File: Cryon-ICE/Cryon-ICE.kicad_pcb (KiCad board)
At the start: 4 copper layers, 34.3 x 63 mm, 207 parts, among them J101 Conn_02x32_Row_Letter_First, J302 10155435-00011LF, J501 TC2050, Q301 DMG1012T, U101 MPFS025T-FCVG484I, U301 PTN5150AHXMP, U302 USB3340-EZK-TR, U303 TPS2051BDR, U401 74LVC1G125, U402 74LVC1G125, U403 74LVC1G125, U404 74LVC1G125, U405 74LVC1G125, U406 74LVC1G125, U407 74LVC1G125, U408 74LVC1G125, U409 74LVC1G125, U410 74LVC1G125, U411 74LVC1G125, U412 74LVC1G125, U413 74LVC1G125, U414 74LVC1G125, U415 74LVC1G125, U416 74LVC1G125, U417 74LVC1G125, U418 74LVC1G125, U419 74LVC1G125, U420 74LVC1G125, U421 74LVC1G125, U422 74LVC1G125, U423 74LVC1G125, U424 74LVC1G125, U425 74LVC1G125, U426 74LVC1G125, U427 74LVC1G125, U428 74LVC1G125, U429 74LVC1G125, U430 74LVC1G125, U431 74LVC1G125, U432 74LVC1G125, U433 74LVC1G125, U434 74LVC1G125, U435 74LVC1G125, U436 74LVC1G125, U437 74LVC1G125, U438 74LVC1G125, U439 74LVC1G125, U440 74LVC1G125, U441 74LVC1G125, U442 74LVC1G125, U443 74LVC1G125, U444 74LVC1G125, U445 74LVC1G125, U446 74LVC1G125, U447 74LVC1G125, U448 74LVC1G125, U449 74LVC1G125, U450 74LVC1G125, U451 74LVC1G125, U452 74LVC1G125, U453 74LVC1G125, U454 74LVC1G125, U455 74LVC1G125, U456 74LVC1G125, U457 74LVC1G125, U458 74LVC1G125, U459 74LVC1G125, U460 74LVC1G125, U461 74LVC1G125, U462 74LVC1G125, U463 74LVC1G125, U464 74LVC1G125, U501 W25Q128JVS, U601 D1621XM4CDGVI-U, Y301 12.88481

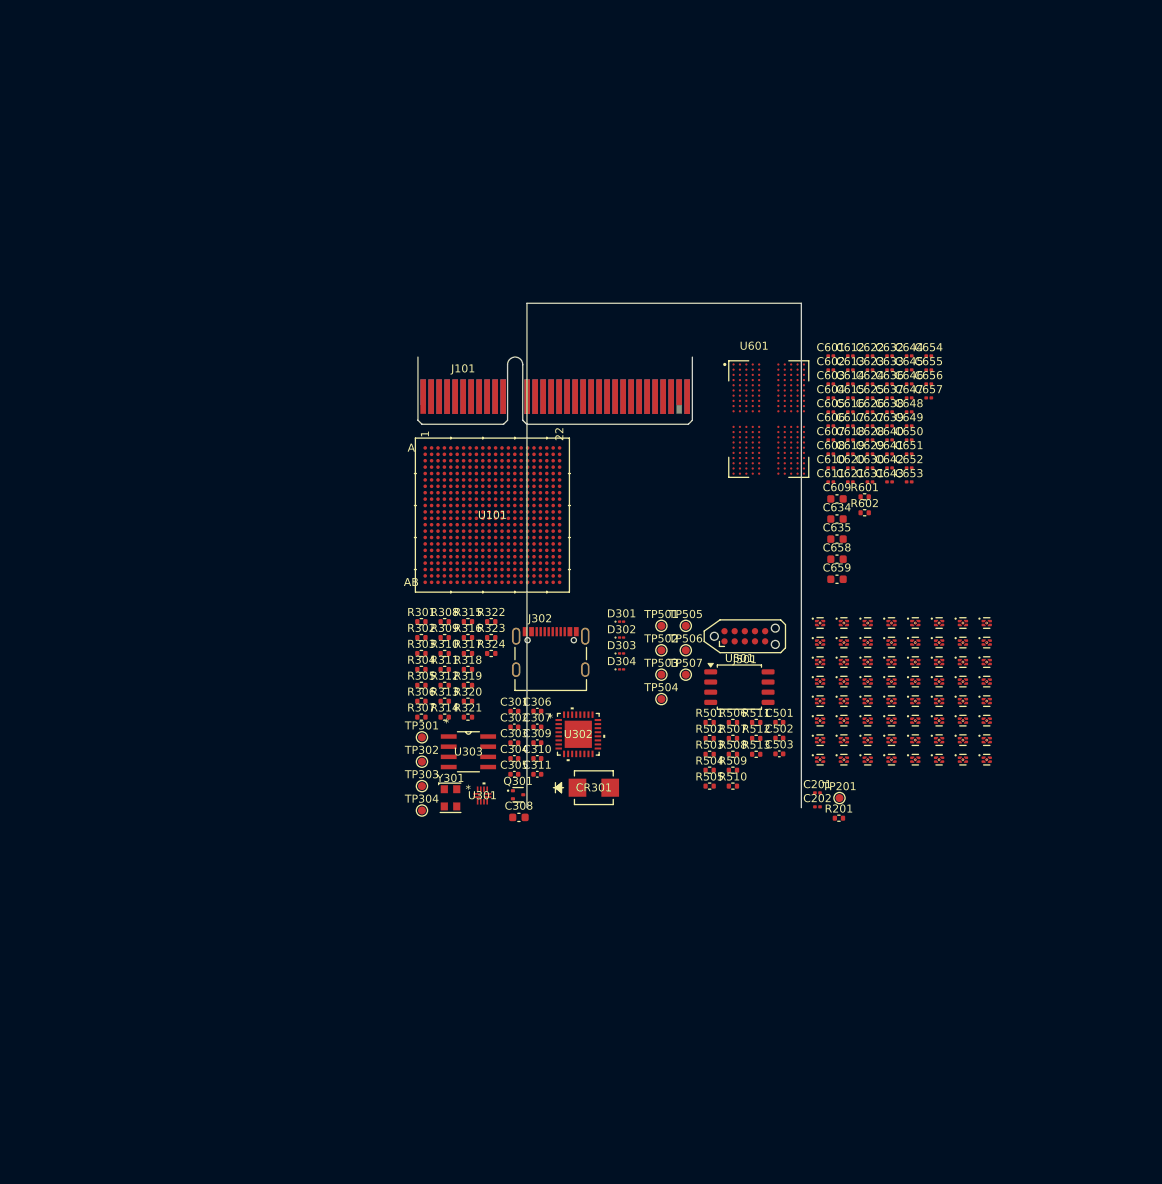
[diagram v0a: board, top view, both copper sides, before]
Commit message: Added micro-sd to schematic
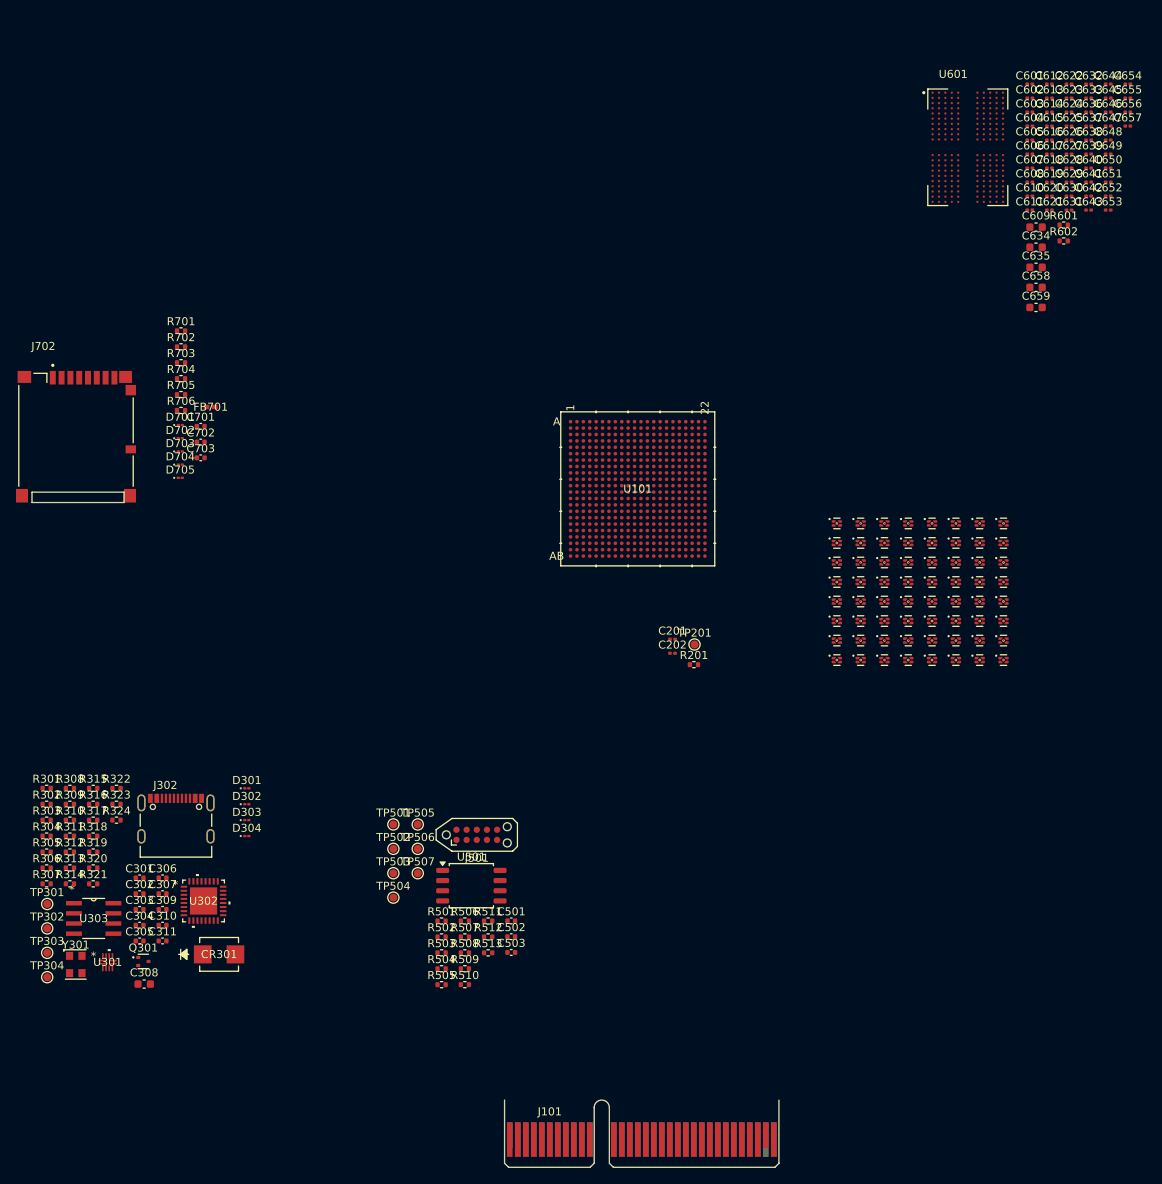
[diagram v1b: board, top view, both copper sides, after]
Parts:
- added C701: 1uF, Capacitor_SMD:C_0402_1005Metric, F.Cu at (89.8, 92.6)
- added C702: 100nF, Capacitor_SMD:C_0402_1005Metric, F.Cu at (89.8, 94.5)
- added C703: 100nF, Capacitor_SMD:C_0402_1005Metric, F.Cu at (89.8, 96.5)
- added D701: GSEPD15B0005, Cryon_Library:D_GSEPD15B0005_01005_0402Metric, F.Cu at (87.2, 92.4)
- added D702: GSEPD15B0005, Cryon_Library:D_GSEPD15B0005_01005_0402Metric, F.Cu at (87.2, 94.1)
- added D703: GSEPD15B0005, Cryon_Library:D_GSEPD15B0005_01005_0402Metric, F.Cu at (87.2, 95.7)
- added D704: GSEPD15B0005, Cryon_Library:D_GSEPD15B0005_01005_0402Metric, F.Cu at (87.2, 97.4)
- added D705: GSEPD15B0005, Cryon_Library:D_GSEPD15B0005_01005_0402Metric, F.Cu at (87.2, 99.0)
- added FB701: 120R-1.3A;0402, Cryon_Library:BLM15P_FBD, F.Cu at (91.0, 90.2)
- added J702: MSD-7-A, Cryon_Library:CUI_MSD-7-A, F.Cu at (74.2, 94.0)
- added R701: 10k, Resistor_SMD:R_0402_1005Metric, F.Cu at (87.3, 80.7)
- added R702: 10k, Resistor_SMD:R_0402_1005Metric, F.Cu at (87.3, 82.6)
- added R703: 10k, Resistor_SMD:R_0402_1005Metric, F.Cu at (87.3, 84.6)
- added R704: 10k, Resistor_SMD:R_0402_1005Metric, F.Cu at (87.3, 86.6)
- added R705: 10k, Resistor_SMD:R_0402_1005Metric, F.Cu at (87.3, 88.6)
- added R706: 33R, Resistor_SMD:R_0402_1005Metric, F.Cu at (87.3, 90.6)
- moved J101 93.5 mm to (128.4, 181.8)
- moved J302 51.3 mm to (86.7, 143.8)
- moved U301 51.3 mm to (78.1, 159.6)
- moved U302 51.3 mm to (90.1, 151.9)
- moved C301 51.3 mm to (82.1, 149.0)
- moved C302 51.3 mm to (82.1, 151.0)
- moved C303 51.3 mm to (82.1, 153.0)
- moved C304 51.3 mm to (82.1, 154.9)
- moved C305 51.3 mm to (82.1, 156.9)
- moved C306 51.3 mm to (85.0, 149.0)
- moved C307 51.3 mm to (85.0, 151.0)
- moved C309 51.3 mm to (85.0, 153.0)
- moved C310 51.3 mm to (85.0, 154.9)
- moved C311 51.3 mm to (85.0, 156.9)
- moved CR301 51.3 mm to (92.1, 158.6)
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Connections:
- U101 pad A2: unconnected-(U101E-MSSIO33B2-PadA2) -> /eMMC_SD/ADC_MISO
- U101 pad B2: unconnected-(U101E-MSSIO32B2-PadB2) -> /eMMC_SD/ADC_MOSI
- U101 pad C7: unconnected-(U101B-GPIO39NB1-PadC7) -> /SD_DET
- U101 pad E5: unconnected-(U101E-MSSIO30B2-PadE5) -> /eMMC_SD/ADC_SCK
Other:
- board size 34.3 x 63 mm -> 34.3 x 8.4 mm

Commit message: Added eMMC
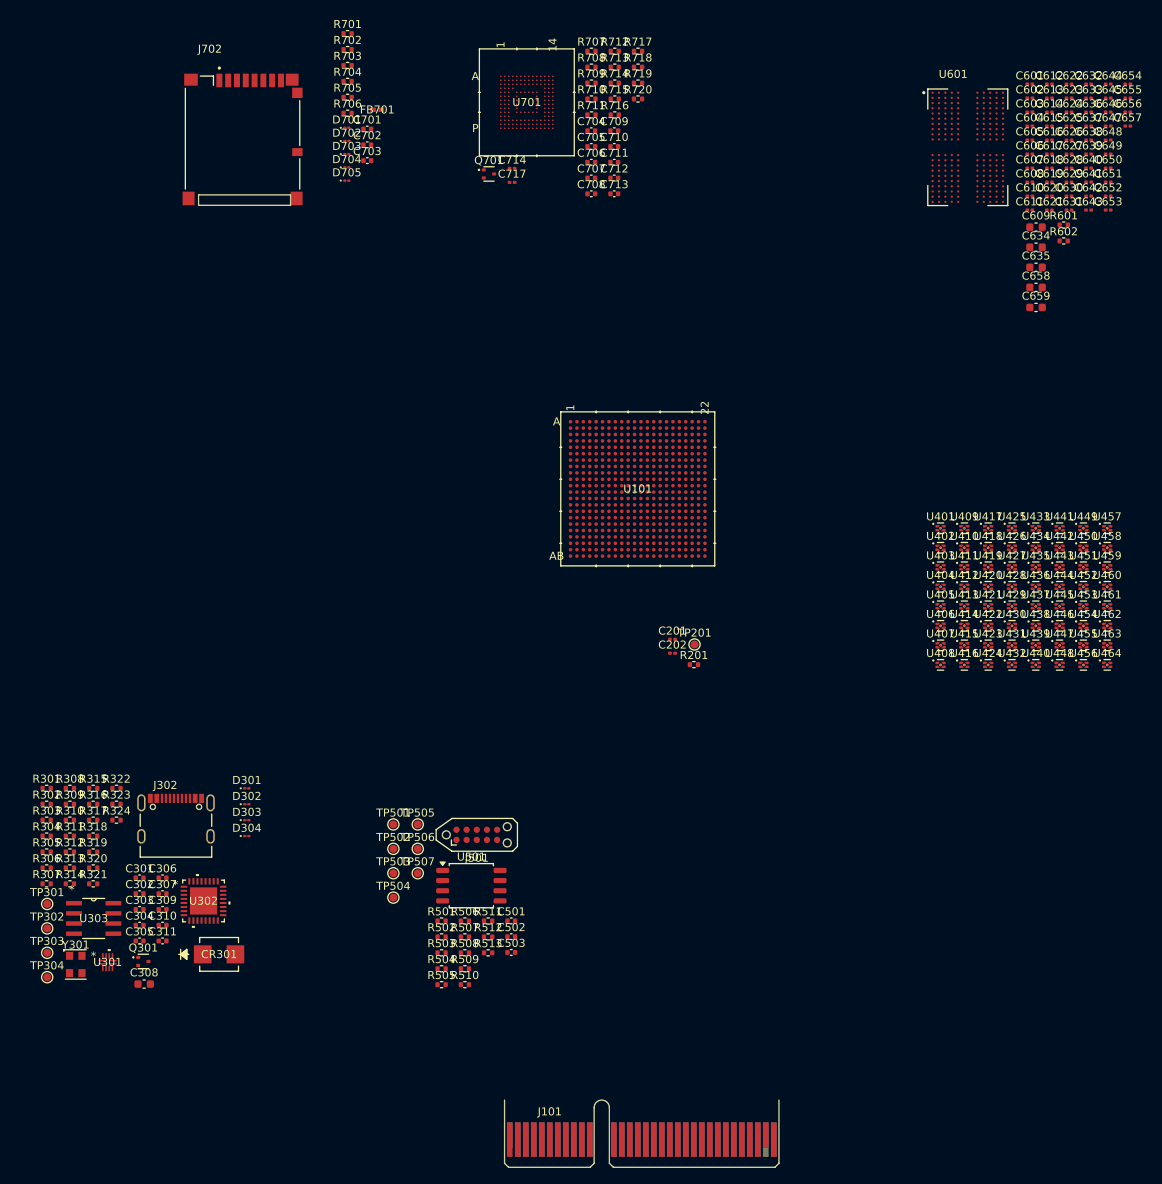
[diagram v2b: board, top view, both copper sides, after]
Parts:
- added C704: 100nF, Capacitor_SMD:C_0402_1005Metric, F.Cu at (138.6, 55.6)
- added C705: 100nF, Capacitor_SMD:C_0402_1005Metric, F.Cu at (138.6, 57.6)
- added C706: 100nF, Capacitor_SMD:C_0402_1005Metric, F.Cu at (138.6, 59.6)
- added C707: 100nF, Capacitor_SMD:C_0402_1005Metric, F.Cu at (138.6, 61.5)
- added C708: 100nF, Capacitor_SMD:C_0402_1005Metric, F.Cu at (138.6, 63.5)
- added C709: 100nF, Capacitor_SMD:C_0402_1005Metric, F.Cu at (141.5, 55.6)
- added C710: 100nF, Capacitor_SMD:C_0402_1005Metric, F.Cu at (141.5, 57.6)
- added C711: 100nF, Capacitor_SMD:C_0402_1005Metric, F.Cu at (141.5, 59.6)
- added C712: 100nF, Capacitor_SMD:C_0402_1005Metric, F.Cu at (141.5, 61.5)
- added C713: 100nF, Capacitor_SMD:C_0402_1005Metric, F.Cu at (141.5, 63.5)
- added C714: 4.7uF, Capacitor_SMD:C_0201_0603Metric, F.Cu at (128.7, 60.3)
- added C717: 4.7uF, Capacitor_SMD:C_0201_0603Metric, F.Cu at (128.7, 62.1)
- added Q701: DMG1012T, Cryon_Library:DMG1012-SOT-523, F.Cu at (125.8, 61.0)
- added R707: 10k, Resistor_SMD:R_0402_1005Metric, F.Cu at (138.6, 45.7)
- added R708: 10k, Resistor_SMD:R_0402_1005Metric, F.Cu at (138.6, 47.7)
- added R709: 49.9k, Resistor_SMD:R_0402_1005Metric, F.Cu at (138.6, 49.7)
- added R710: 49.9k, Resistor_SMD:R_0402_1005Metric, F.Cu at (138.6, 51.7)
- added R711: 49.9k, Resistor_SMD:R_0402_1005Metric, F.Cu at (138.6, 53.7)
- added R712: 49.9k, Resistor_SMD:R_0402_1005Metric, F.Cu at (141.5, 45.7)
- added R713: 49.9k, Resistor_SMD:R_0402_1005Metric, F.Cu at (141.5, 47.7)
- added R714: 49.9k, Resistor_SMD:R_0402_1005Metric, F.Cu at (141.5, 49.7)
- added R715: 49.9k, Resistor_SMD:R_0402_1005Metric, F.Cu at (141.5, 51.7)
- added R716: 49.9k, Resistor_SMD:R_0402_1005Metric, F.Cu at (141.5, 53.7)
- added R717: 49.9k, Resistor_SMD:R_0402_1005Metric, F.Cu at (144.4, 45.7)
- added R718: 49.9k, Resistor_SMD:R_0402_1005Metric, F.Cu at (144.4, 47.7)
- added R719: 0R, Resistor_SMD:R_0402_1005Metric, F.Cu at (144.4, 49.7)
- added R720: 10K, Resistor_SMD:R_0402_1005Metric, F.Cu at (144.4, 51.7)
- added U701: MX52LM08A11XVI, Cryon_Library:153BGA_11p5x13x1_MAC, F.Cu at (130.5, 52.1)
- moved C701 42.6 mm to (110.6, 55.4)
- moved R701 42.6 mm to (108.1, 43.5)
- moved C702 42.6 mm to (110.6, 57.4)
- moved C703 42.6 mm to (110.6, 59.4)
- moved D701 42.6 mm to (108.0, 55.3)
- moved D703 42.6 mm to (108.0, 58.6)
- moved D704 42.6 mm to (108.0, 60.2)
- moved FB701 42.6 mm to (111.8, 53.0)
- moved J702 42.6 mm to (95.0, 56.8)
- moved R702 42.6 mm to (108.1, 45.5)
- moved R704 42.6 mm to (108.1, 49.5)
- moved R705 42.6 mm to (108.1, 51.5)
- moved D702 42.6 mm to (108.0, 56.9)
- moved D705 42.6 mm to (108.0, 61.9)
- moved R703 42.6 mm to (108.1, 47.5)
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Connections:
- J702 pad SW_A2: /SD_DET -> GND
- U101 pad H1: unconnected-(U101E-MSSIO2B4-PadH1) -> /eMMC_SD/EMMC_DATA0
- U101 pad H2: unconnected-(U101E-MSSIO11B4-PadH2) -> /eMMC_SD/EMMC_DATA7
- U101 pad H4: unconnected-(U101E-MSSIO7B4-PadH4) -> /eMMC_SD/EMMC_RSTn
- U101 pad H5: unconnected-(U101E-MSSIO12B4-PadH5) -> /eMMC_SD/SDCARD_CS
- U101 pad H6: unconnected-(U101E-MSSIO9B4-PadH6) -> /eMMC_SD/EMMC_DATA5
- U101 pad J1: unconnected-(U101E-MSSIO0B4-PadJ1) -> /eMMC_SD/EMMC_CLK
- U101 pad J2: unconnected-(U101E-MSSIO13B4-PadJ2) -> /USER_BUTTON
- U101 pad J3: unconnected-(U101E-MSSIO10B4-PadJ3) -> /eMMC_SD/EMMC_DATA6
- U101 pad J4: unconnected-(U101E-MSSIO3B4-PadJ4) -> /eMMC_SD/EMMC_DATA1
- U101 pad J6: unconnected-(U101E-MSSIO8B4-PadJ6) -> /eMMC_SD/EMMC_DATA4
- U101 pad J7: unconnected-(U101E-MSSIO5B4-PadJ7) -> /eMMC_SD/EMMC_DATA3
- U101 pad K3: unconnected-(U101E-MSSIO6B4-PadK3) -> /eMMC_SD/EMMC_DQ
- U101 pad K4: unconnected-(U101E-MSSIO4B4-PadK4) -> /eMMC_SD/EMMC_DATA2
- U101 pad K5: unconnected-(U101E-MSSIO1B4-PadK5) -> /eMMC_SD/EMMC_CMD
